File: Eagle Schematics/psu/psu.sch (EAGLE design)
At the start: 14 parts, among them IC1 7805T, IC2 7805T, IC3 REG1117

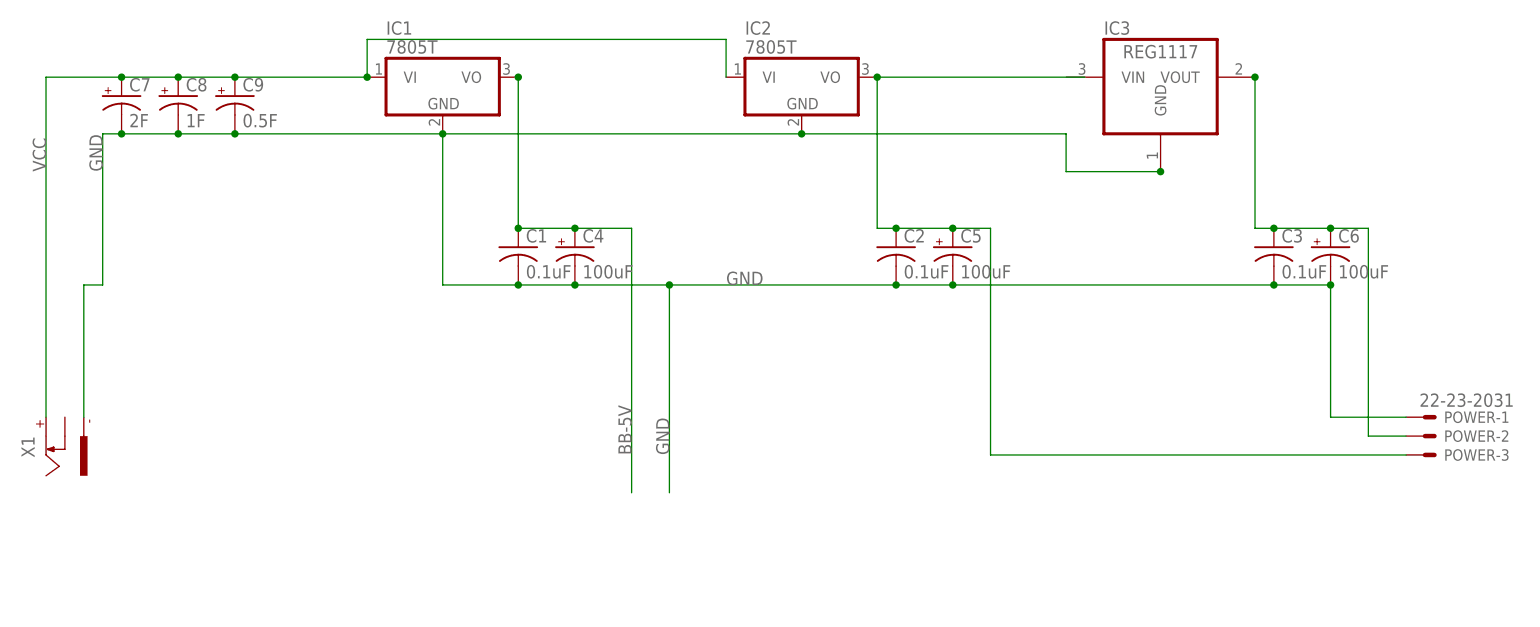
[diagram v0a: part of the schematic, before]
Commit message: Added PSU and entity module schematic
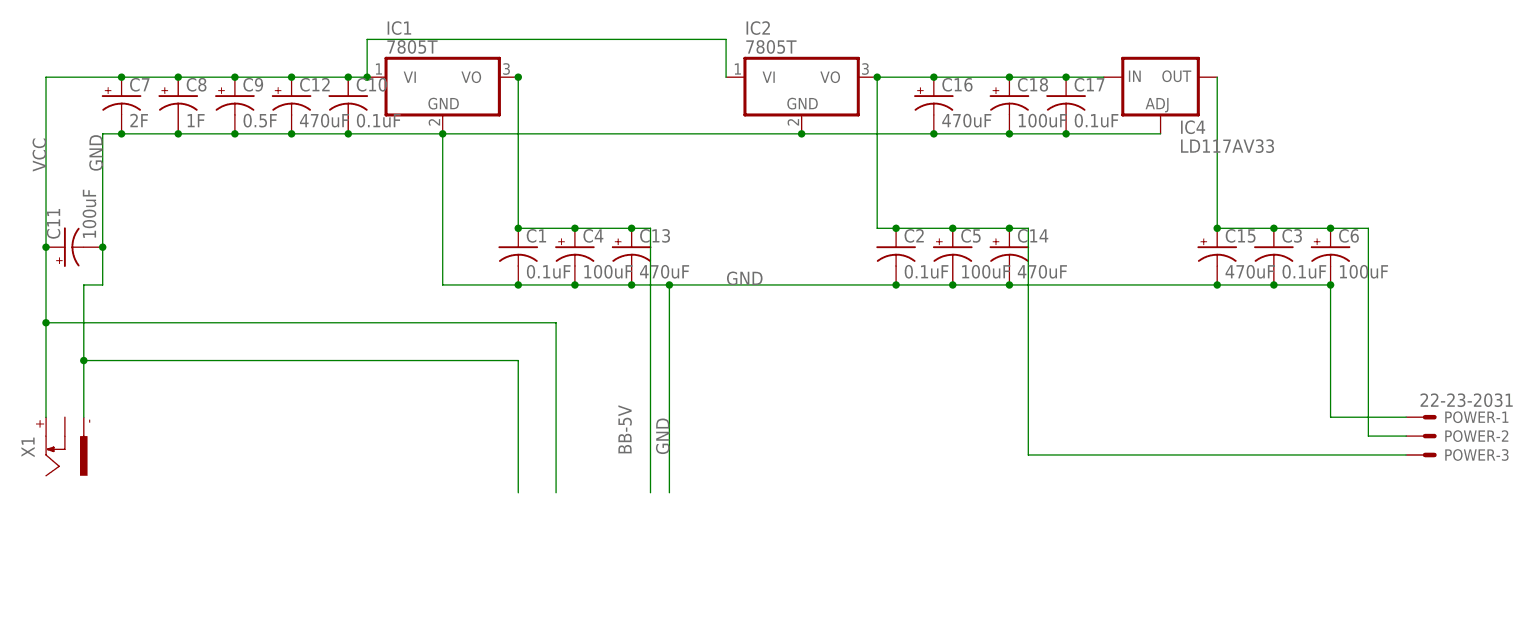
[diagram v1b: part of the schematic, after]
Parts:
- removed IC3: REG1117, burr-brown:REG1117
- added C10, C17: 0.1uF, rcl:C-US025-025X050
- added C11, C18: 100uF, rcl:CPOL-USE2-4
- added C12, C13, C14, C15, C16: 470uF, rcl:CPOL-USE2-4
- added IC4: LD117AV33, v-reg:LD117AV33
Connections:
- net BB-5V: now also C13.+
- net GND: now also C10.2, C11.-, C12.-, C13.-, C14.-, C15.-, C16.-, C17.2, C18.-, IC4.ADJ; no longer IC3.GND
- net N$1: now also C14.+, C16.+, C17.1, C18.+, IC4.IN
- net N$3: now also C15.+, IC4.OUT; no longer IC3.VOUT
- net VCC: now also C10.1, C11.+, C12.+

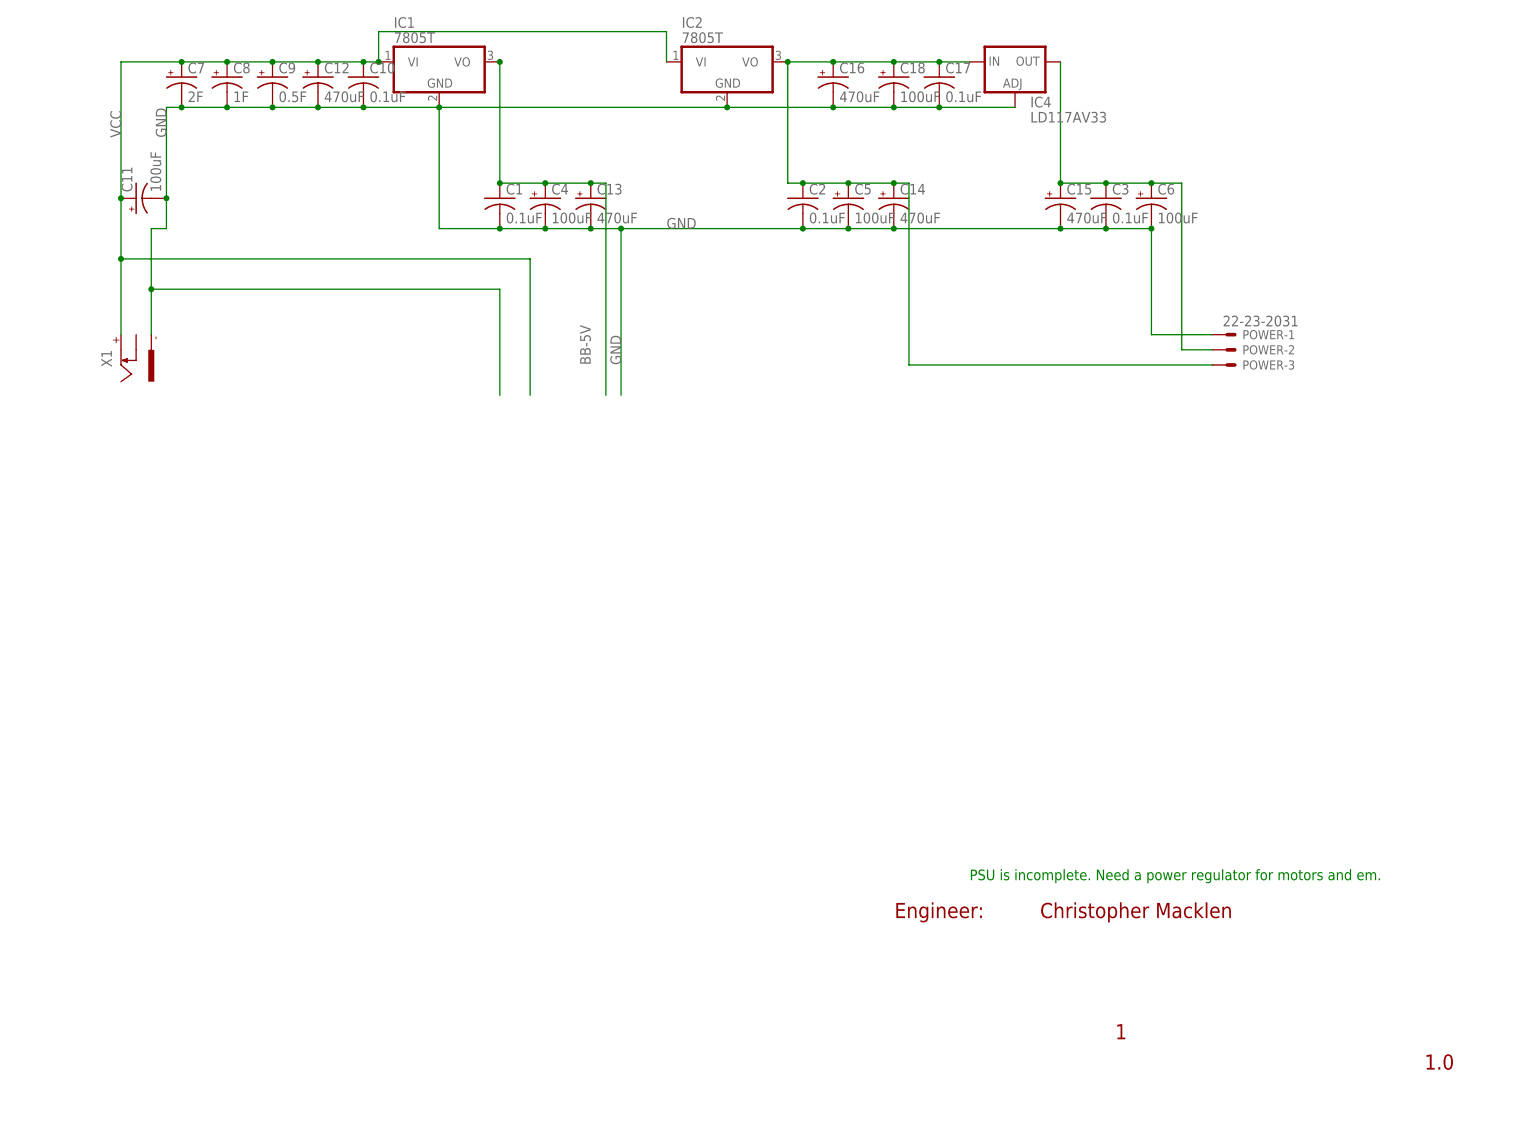
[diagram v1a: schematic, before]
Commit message: Updated PSU schematic and documentation
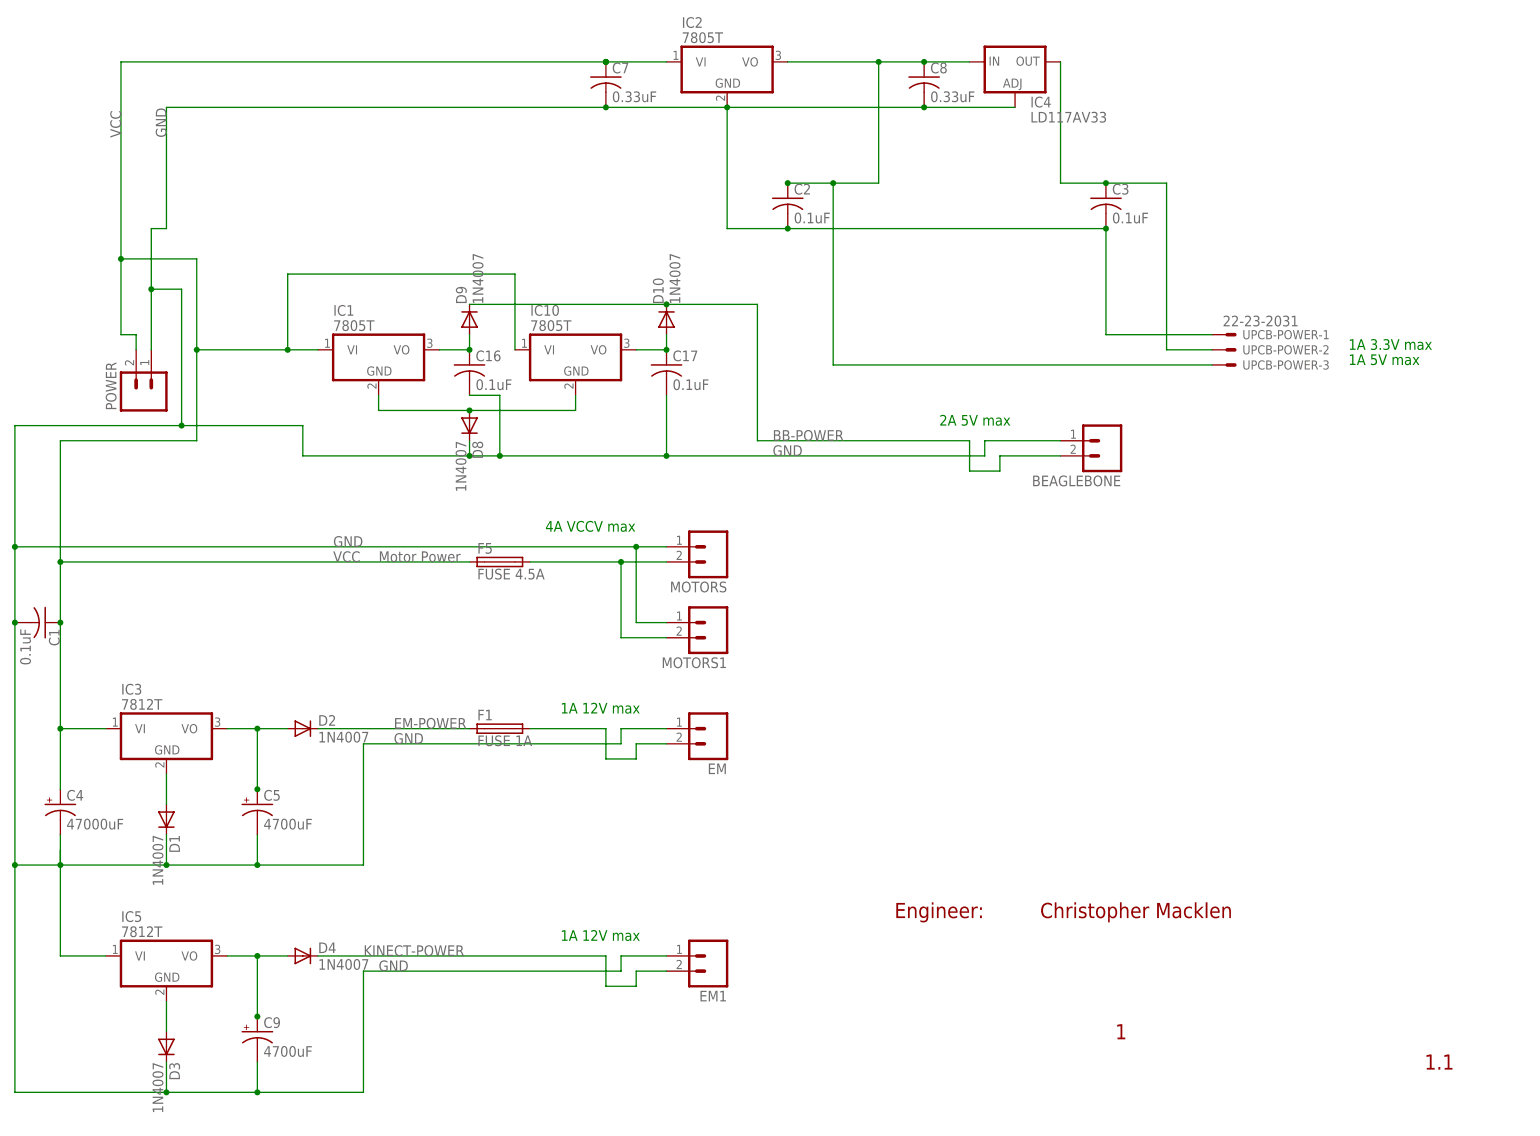
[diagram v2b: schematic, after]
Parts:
- removed C10: 0.1uF, rcl:C-US025-025X050
- removed C11, C18, C6: 100uF, rcl:CPOL-USE2-4
- removed C12, C13, C14, C15: 470uF, rcl:CPOL-USE2-4
- removed X1: (no value), con-conrad:737992-55
- added BEAGLEBONE, EM, EM1, MOTORS, MOTORS1: (no value), con-amp-quick:M02
- added D1, D10, D2, D3, D4, D8, D9: 1N4007, diode:1N4004
- added F1: FUSE 1A, fuse:FUSEPICOFUSE
- added F5: FUSE 4.5A, fuse:FUSEPICOFUSE
- added IC10: 7805T, linear:7805T
- added IC3, IC5: 7812T, linear:7812T
- added UPCB-POWER: 22-23-2031, con-molex:22-23-2031
- C16: value 470uF -> 0.1uF; device rcl:CPOL-USE2-4 -> rcl:C-US025-025X050
- C4: value 100uF -> 47000uF; device rcl:CPOL-USE2-4 -> rcl:CPOL-USE2,5-6E
- C5: value 100uF -> 4700uF; device rcl:CPOL-USE2-4 -> rcl:CPOL-USE2,5-6E
- C7: value 2F -> 0.33uF; device rcl:CPOL-USE2-4 -> rcl:C-US025-025X050
- C8: value 1F -> 0.33uF; device rcl:CPOL-USE2-4 -> rcl:C-US025-025X050
- C9: value 0.5F -> 4700uF; device rcl:CPOL-USE2-4 -> rcl:CPOL-USE2,5-6E
- POWER: value 22-23-2031 -> (none); device con-molex:22-23-2031 -> con-amp-quick:M02; OC_FARNELL (none) -> unknown; OC_NEWARK (none) -> unknown
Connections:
- removed net BB-5V: C1.1, C13.+, C4.+, IC1.VO
- removed net N$1: C14.+, C16.+, C17.1, C18.+, C2.1, C5.+, IC2.VO, IC4.IN, POWER-3.S
- new net 12V: C5.+, D2.A, IC3.VO
- new net 12V1: C9.+, D4.A, IC5.VO
- new net 3.3V: C3.1, IC4.OUT, UPCB-POWER-2.S
- new net 5-1A,1: C16.1, D9.A, IC1.VO
- new net 5V: C2.1, C8.1, IC2.VO, IC4.IN, UPCB-POWER-3.S
- new net 5V-1A,2: C17.1, D10.A, IC10.VO
- new net BB-POWER: BEAGLEBONE.2, D10.C, D9.C
- new net EM-POWER: D2.C, F1.1
- new net GND-IC1: D3.A, IC5.GND
- new net GND-IC1,10: D8.A, IC1.GND, IC10.GND
- new net GND-IC3: D1.A, IC3.GND
- new net KINECT-POWER: D4.C, EM1.2
- new net N$2: F5.2, MOTORS.2, MOTORS1.2
- new net VCC1: IC5.VI
- net GND: now also BEAGLEBONE.1, C16.2, C7.2, C8.2, D1.C, D3.C, D8.C, EM.1, EM1.1, MOTORS.1, MOTORS1.1, POWER.1, UPCB-POWER-1.S; no longer C10.2, C11.-, C12.-, C13.-, C14.-, C15.-, C16.-, C18.-, C6.-, C7.-, C8.-, IC1.GND, POWER-1.S, X1.-1
- net N$3: now also EM.2, F1.2; no longer C15.+, C3.1, C6.+, IC4.OUT, POWER-2.S
- net VCC: now also C1.1, C4.+, C7.1, F5.1, IC10.VI, IC3.VI, POWER.2; no longer C10.1, C11.+, C12.+, C7.+, C8.+, C9.+, X1.+
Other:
- note added: "1.1"
- note added: "1A 12V max"
- note added: "1A 3.3V max"
- note added: "1A 5V max"
- note added: "2A 5V max"
- note added: "4A VCCV max"
- note added: "Motor Power"
- note removed: "1.0"
- note removed: "PSU is incomplete. Need a power regulator for motors and em."
- moved on the sheet: C1, C17, C2, C4, C5, C9, IC1

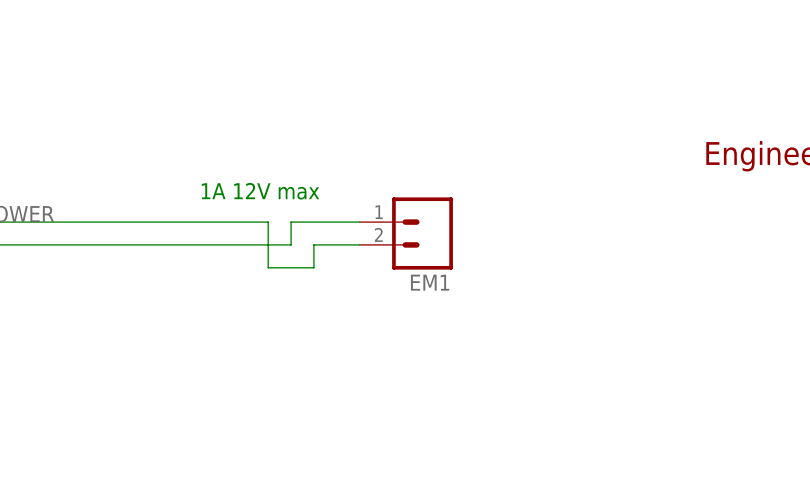
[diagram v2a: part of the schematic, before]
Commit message: Finalized PSU schematic
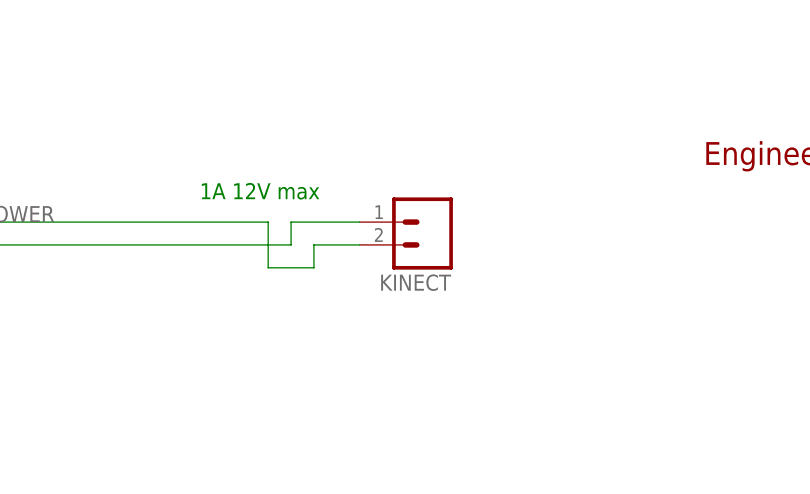
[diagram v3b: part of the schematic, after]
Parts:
- renumbered EM1 to KINECT
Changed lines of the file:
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@@
 <part name="C9" library="rcl" deviceset="CPOL-US" device="E2,5-6E" value="4700uF"/>
 <part name="D4" library="diode" deviceset="1N4004" device="" value="1N4007"/>
-<part name="EM1" library="con-amp-quick" deviceset="M02" device=""/>
+<part name="KINECT" library="con-amp-quick" deviceset="M02" device=""/>
 </parts>
 <sheets>
@@
 <instance part="C9" gate="G$1" x="43.18" y="12.7"/>
 <instance part="D4" gate="1" x="50.8" y="25.4"/>
-<instance part="EM1" gate="G$1" x="119.38" y="25.4" rot="R180"/>
+<instance part="KINECT" gate="G$1" x="119.38" y="25.4" rot="R180"/>
 </instances>
 <busses>
@@
 <wire x1="60.96" y1="22.86" x2="104.14" y2="22.86" width="0.1524" layer="91"/>
 <wire x1="104.14" y1="22.86" x2="104.14" y2="25.4" width="0.1524" layer="91"/>
-<pinref part="EM1" gate="G$1" pin="1"/>
+<pinref part="KINECT" gate="G$1" pin="1"/>
 <wire x1="104.14" y1="25.4" x2="111.76" y2="25.4" width="0.1524" layer="91"/>
 <wire x1="2.54" y1="40.64" x2="2.54" y2="2.54" width="0.1524" layer="91"/>
@@
 <wire x1="101.6" y1="20.32" x2="106.68" y2="20.32" width="0.1524" layer="91"/>
 <wire x1="106.68" y1="20.32" x2="106.68" y2="22.86" width="0.1524" layer="91"/>
-<pinref part="EM1" gate="G$1" pin="2"/>
+<pinref part="KINECT" gate="G$1" pin="2"/>
 <wire x1="106.68" y1="22.86" x2="111.76" y2="22.86" width="0.1524" layer="91"/>
 </segment>
